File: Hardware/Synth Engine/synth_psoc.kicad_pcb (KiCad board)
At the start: 2 copper layers, 233 parts, among them J1 Barrel_Jack, J10 Conn_01x13, J11 Conn_01x13, J13 Conn_01x05, J14 Conn_01x05, J15 Conn_01x05, J16 Conn_01x05, J2 Audio-Jack-2_Switch, J3 SWD_programming, J4 Conn_01x08, J5 Conn_01x02, J6 Conn_01x03, J7 Capsense_buttons, J8 Conn_01x13, J9 Conn_01x13, Q1 MMBT3904-TP, Q2 MMBT3904-TP, Q3 MMBT3904-TP, Q4 MMBT3904-TP, Q5 MMBFJ177, Q6 MMBFJ177, Q7 MMBFJ177, Q8 MMBFJ177, U1 TL074, U2 TL074, U3 TL074, U4 TL074, U5 TL074, U6 CY8C4246AZI-L445, U7 V7805-1000, U8 PT2399, Y1 Crystal

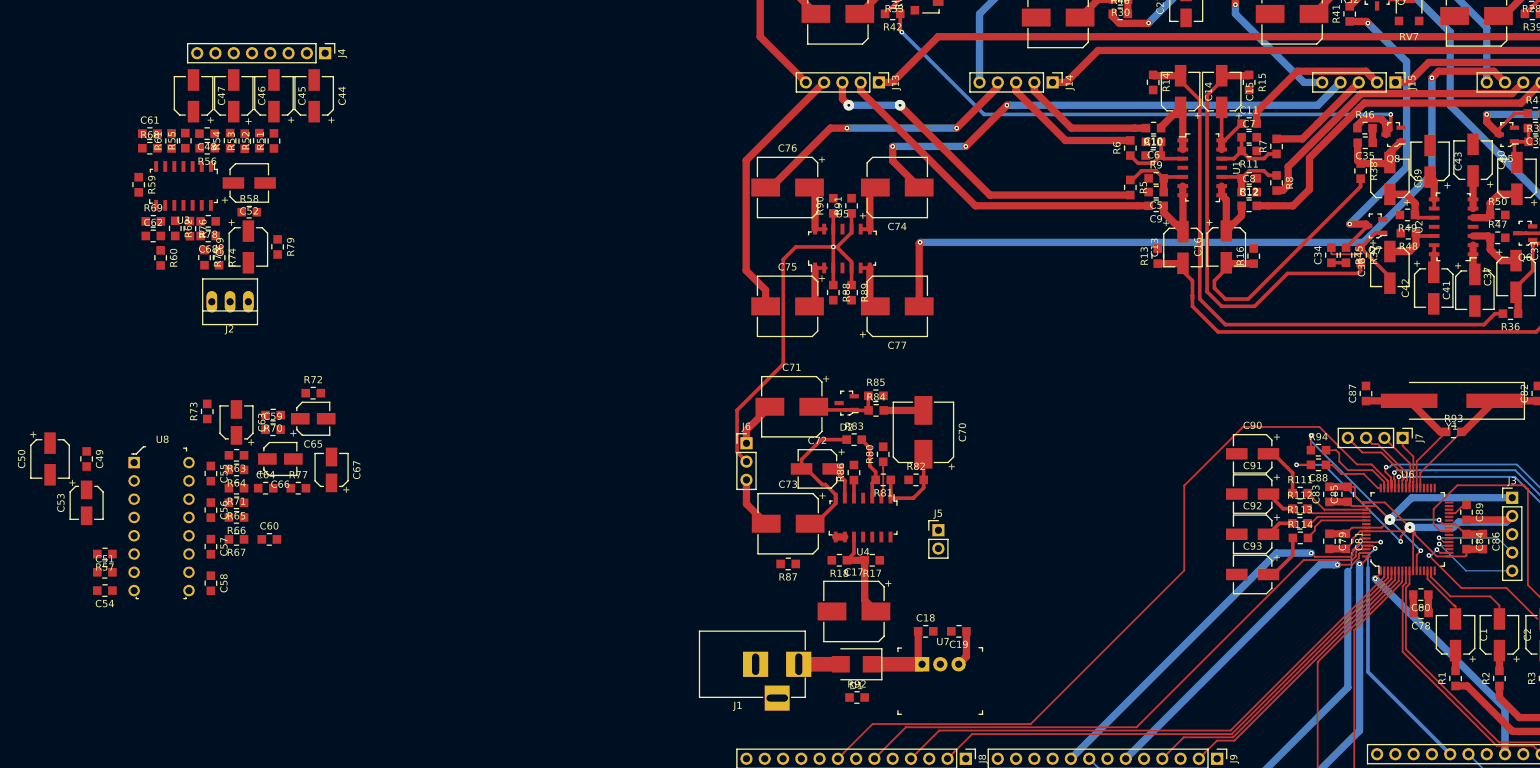
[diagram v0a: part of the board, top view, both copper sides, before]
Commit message: route output mixer. connector placement will probably have to change.
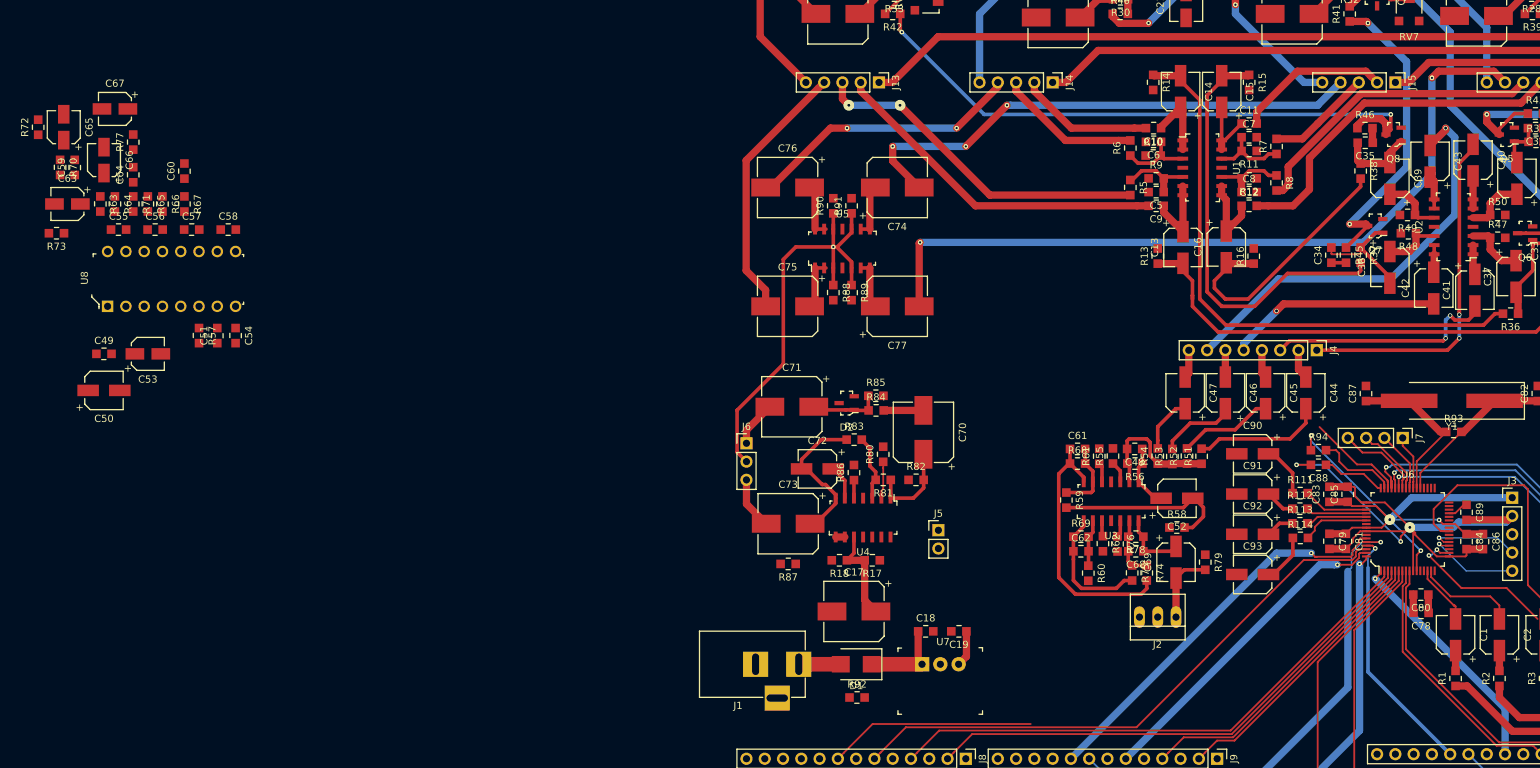
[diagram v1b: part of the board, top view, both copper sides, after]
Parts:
- moved C45 143.8 mm to (74.7, 113.6)
- moved C47 143.8 mm to (63.5, 113.6)
- moved C44 143.8 mm to (80.3, 113.6)
- moved C46 143.8 mm to (69.1, 113.6)
- moved J4 143.8 mm to (81.8, 107.7)
- moved C48 136.1 mm to (56.5, 121.4)
- moved C52 136.1 mm to (62.4, 128.3)
- moved C61 136.1 mm to (48.5, 121.4)
- moved C62 136.1 mm to (49.0, 135.6)
- moved C68 136.1 mm to (56.6, 135.6)
- moved C69 136.1 mm to (62.2, 137.2)
- moved J2 136.1 mm to (62.2, 144.8)
- moved R51 136.1 mm to (65.8, 122.4)
- moved R52 136.1 mm to (63.8, 122.4)
- moved R53 136.1 mm to (61.7, 122.5)
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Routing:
- net /Connectors/osc1_repeat: track 106.5 -> 42.4 mm
- net Net-(C43-Pad2): track 0.00 -> 58.1 mm, vias 0 -> 1
- net Net-(C40-Pad2): track 0.00 -> 48.2 mm, vias 0 -> 2
- net Net-(C61-Pad1): track 0.00 -> 36.6 mm
- net Net-(C41-Pad2): track 0.00 -> 32.6 mm, vias 0 -> 2
- net Net-(C42-Pad2): track 0.00 -> 29.6 mm, vias 0 -> 1
- net /Mixer and Effects/delay_in: track 0.00 -> 24.7 mm
- net Net-(C48-Pad2): track 0.00 -> 18.9 mm
- net Net-(C62-Pad1): track 0.00 -> 18.0 mm
- net Net-(C44-Pad1): track 0.00 -> 18.0 mm
- net Net-(C45-Pad1): track 0.00 -> 13.2 mm
- net Net-(C46-Pad1): track 0.00 -> 10.7 mm
- net Net-(C61-Pad2): track 0.00 -> 10.1 mm
- net Net-(C69-Pad2): track 0.00 -> 9.96 mm
- net Net-(C68-Pad1): track 0.00 -> 9.35 mm
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
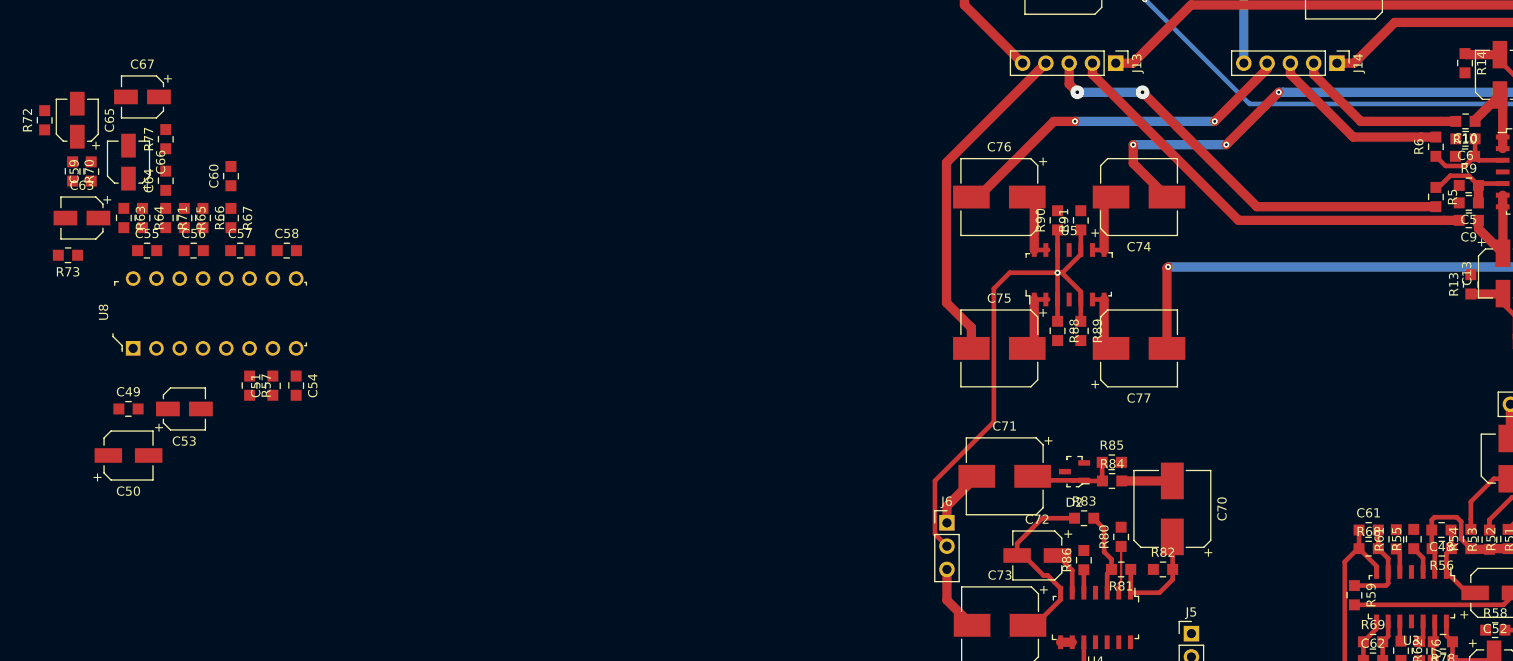
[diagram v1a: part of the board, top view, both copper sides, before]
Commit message: place delay footprints
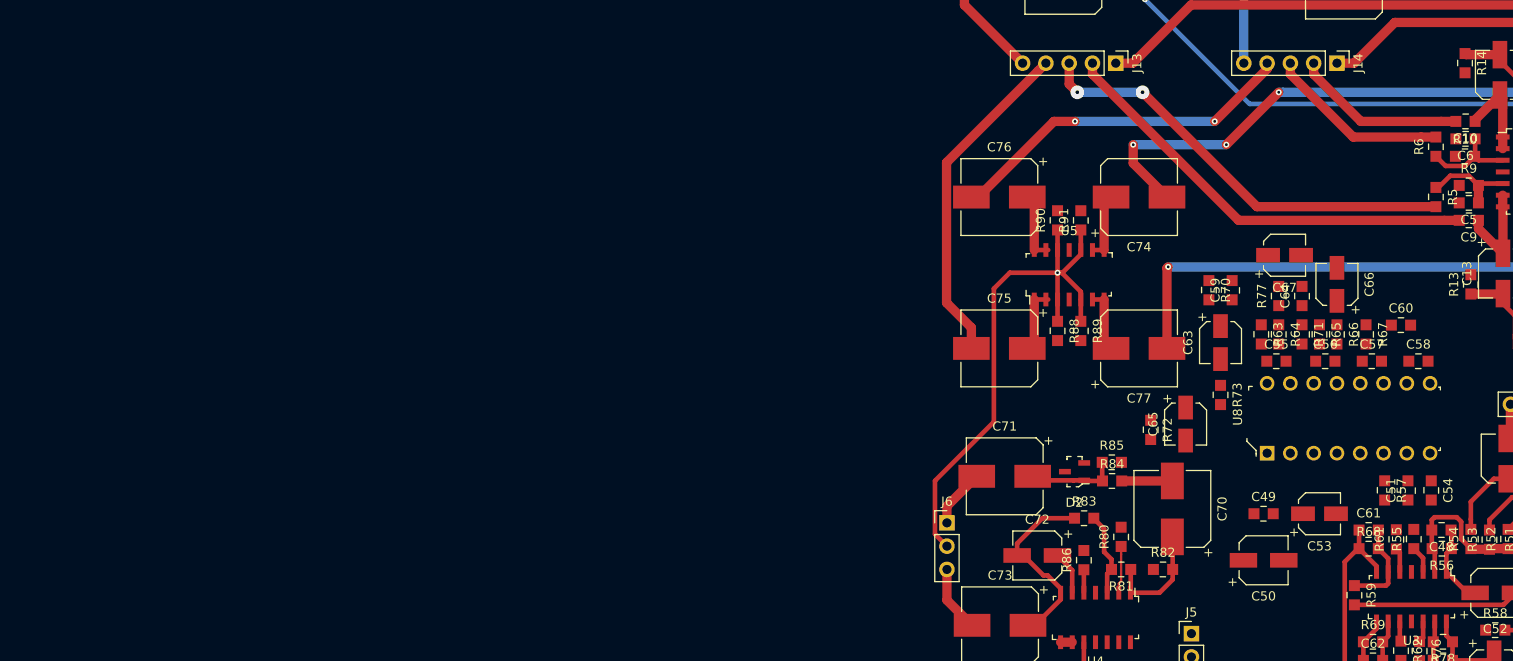
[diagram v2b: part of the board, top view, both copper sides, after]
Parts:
- moved C66 132.5 mm to (45.1, 94.6)
- moved C60 128.7 mm to (52.1, 99.1), turned to 0 degrees
- moved R73 126.7 mm to (32.4, 106.7), turned to 270 degrees
- moved C67 125.8 mm to (39.4, 91.4), turned to 0 degrees
- moved C65 125.4 mm to (28.6, 109.9), turned to 270 degrees
- moved R72 125.3 mm to (24.8, 110.5), turned to 270 degrees
- moved C59 125.1 mm to (33.7, 95.2)
- moved C63 124.9 mm to (32.4, 101.0), turned to 270 degrees
- moved R63 124.7 mm to (36.8, 100.1)
- moved R70 124.6 mm to (31.1, 95.2)
- moved R64 124.6 mm to (38.7, 100.1)
- moved R71 124.6 mm to (41.3, 100.1)
- moved C64 124.6 mm to (41.3, 95.9)
- moved R65 124.5 mm to (43.2, 100.1)
- moved R67 124.5 mm to (48.3, 100.1)
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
